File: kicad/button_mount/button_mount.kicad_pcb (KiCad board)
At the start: 2 copper layers, 8 parts, among them J1 SW Terminal, J2 LED Terminal, SW1 CROWN-SDB-201C

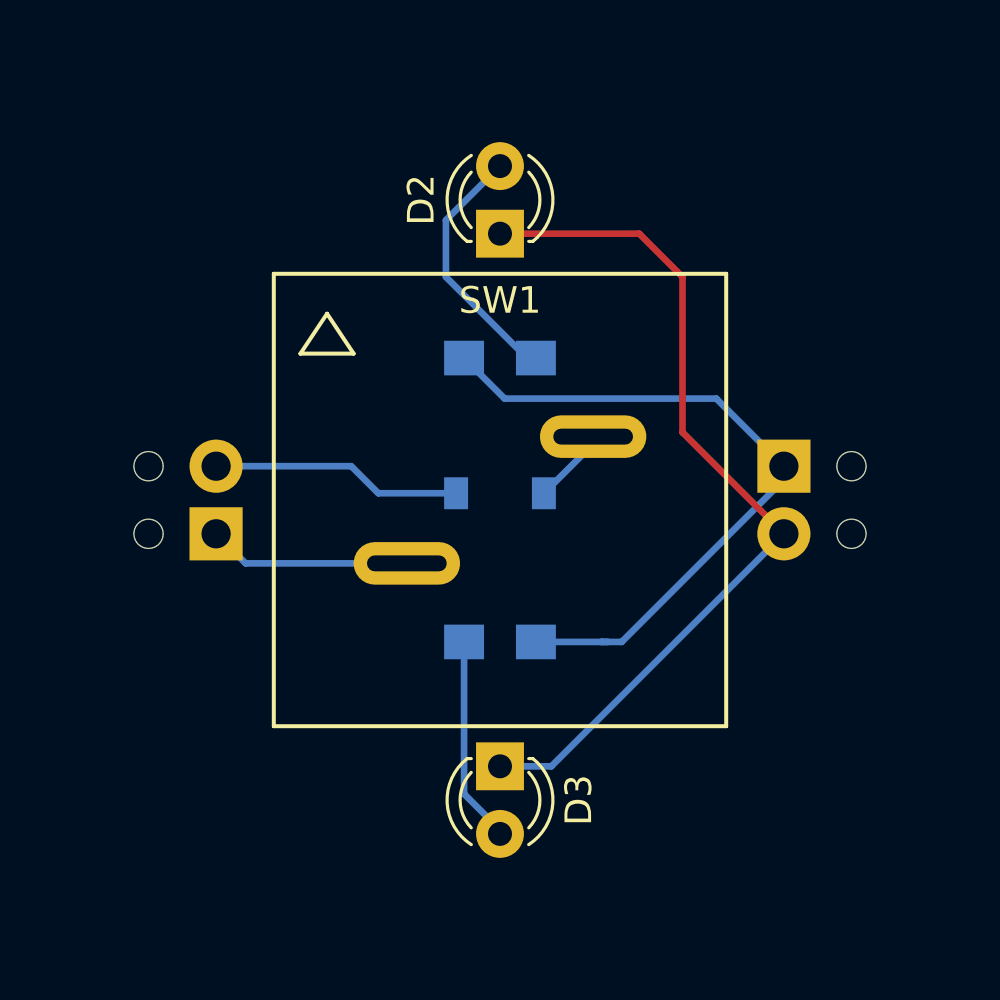
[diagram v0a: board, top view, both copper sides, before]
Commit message: Add Edge.Cuts
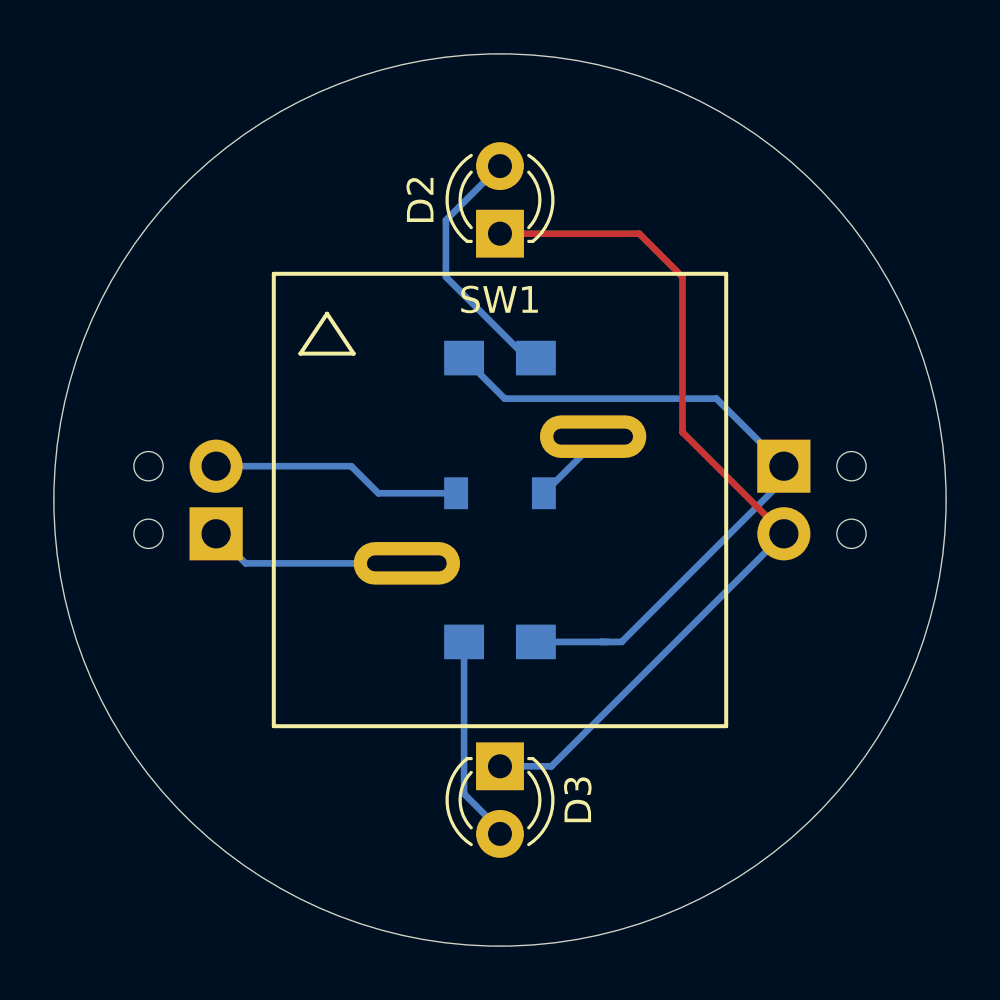
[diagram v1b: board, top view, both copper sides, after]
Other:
- board outline added: 33.5 x 33.5 mm

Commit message: Add more silk / OSHW logo
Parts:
- added G***: OSHW, button_mount:OSHW, B.Cu at (110.2, 98.0)
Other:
- board text added: "BBr1 '21"

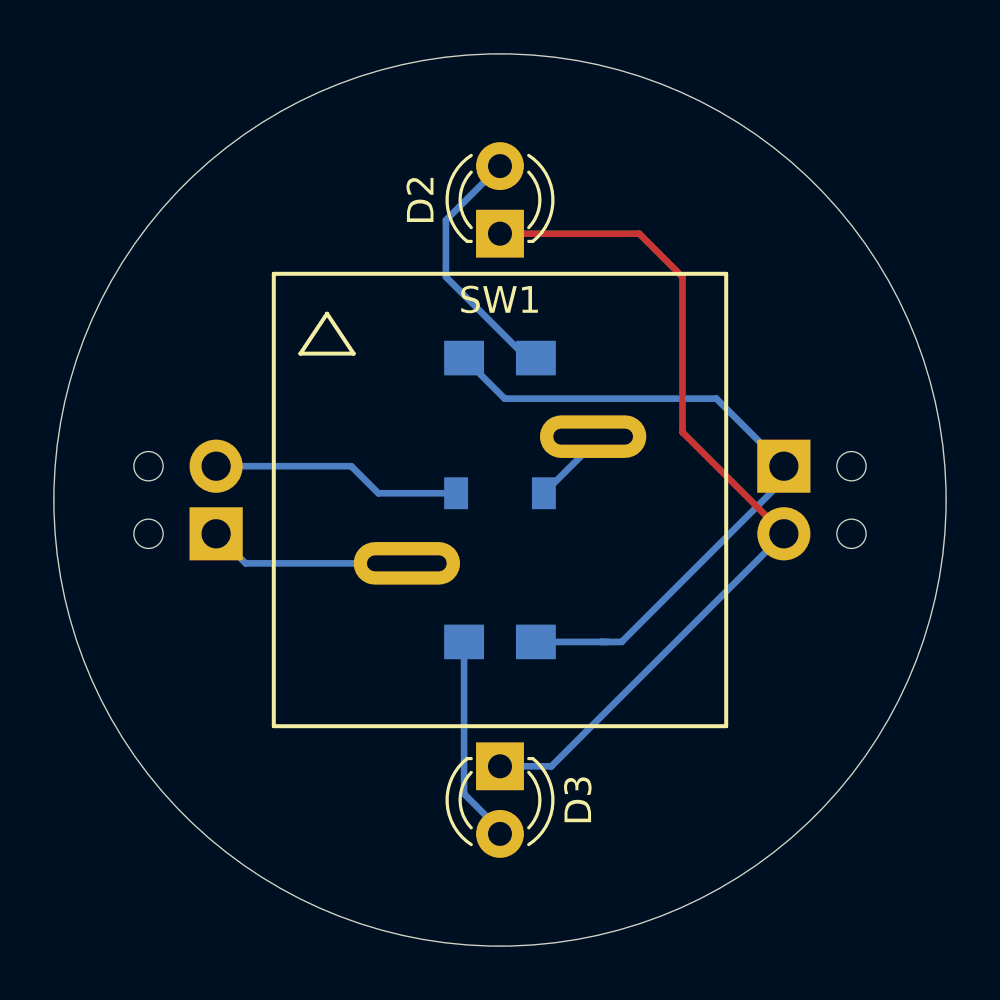
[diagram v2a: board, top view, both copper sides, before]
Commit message: Cancelled BBr1. Updated BBr2 to include 4x term blocks, smaller diam
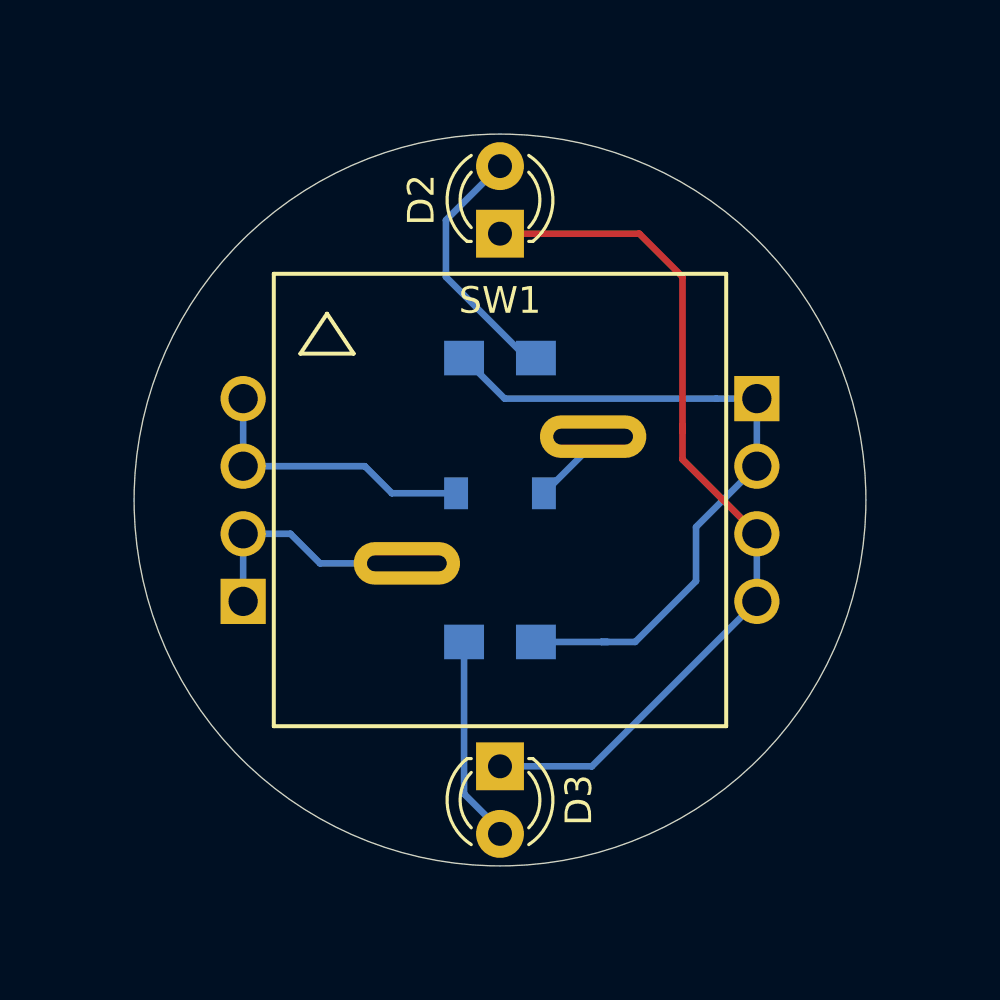
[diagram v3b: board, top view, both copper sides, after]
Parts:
- J1: value SW Terminal -> OSTVN04A150; footprint TerminalBlocks_Phoenix:TerminalBlock_Phoenix_MPT-2.54mm_2pol -> button_mount:OSTVN04A150
- J2: value LED Terminal -> OSTVN04A150; footprint TerminalBlocks_Phoenix:TerminalBlock_Phoenix_MPT-2.54mm_2pol -> button_mount:OSTVN04A150
- moved J2 2.74 mm to (127.5, 85.1)
- moved J1 2.74 mm to (108.2, 92.7)
- moved G*** 2.17 mm to (112.3, 97.3)
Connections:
- J1 pad 2: /COL_OUT -> /ROW_IN
- J2 pad 2: /LED_K -> /LED_A
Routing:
- net /ROW_IN: track 7.63 -> 9.15 mm
- net /COL_OUT: track 9.44 -> 11.0 mm
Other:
- board size 33.5 x 33.5 mm -> 27.5 x 27.5 mm
- board text added: "BBr2 '21"
- board text added: "OD of switch is 27.7mm (r=13.75)"
- board text removed: "BBr1 '21"
